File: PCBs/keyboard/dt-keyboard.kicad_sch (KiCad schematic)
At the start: 87 parts

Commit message: Fixed Keyboard
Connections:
- net Column 10: now also J1.14; no longer J1.10
- net Column 4: now also J1.8; no longer J1.4
- net Column 5: now also J1.9; no longer J1.5
- net Column 6: now also J1.10; no longer J1.6
- net Column 7: now also J1.11; no longer J1.7
- net Column 8: now also J1.12; no longer J1.8
- net Column 9: now also J1.13; no longer J1.9
- net Row 0: now also J1.4; no longer J1.11
- net Row 1: now also J1.5; no longer J1.12
- net Row 2: now also J1.6; no longer J1.13
- net Row 3: now also J1.7; no longer J1.14
- net GND: no longer names the net of J1.15 (MP)
- net GND: no longer J1.16 (MP)
- no-connect marks 0 -> 2
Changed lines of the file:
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@@
 		(color 0 0 0 0)
 	)
+	(no_connect
+		(at 35.56 137.16)
+	)
+	(no_connect
+		(at 35.56 185.42)
+	)
 	(wire
 		(pts
@@
 	(global_label "Row 3"
 		(shape input)
-		(at 43.18 179.07 0)
+		(at 43.18 161.29 0)
 		(fields_autoplaced yes)
 		(effects
@@
 		)
 		(property "Intersheetrefs" "${INTERSHEET_REFS}"
-			(at 52.0918 179.07 0)
+			(at 52.0918 161.29 0)
 			(effects
 				(font
@@
 	(global_label "Column 4"
 		(shape input)
-		(at 43.18 153.67 0)
+		(at 43.18 163.83 0)
 		(fields_autoplaced yes)
 		(effects
@@
 		)
 		(property "Intersheetrefs" "${INTERSHEET_REFS}"
-			(at 55.4178 153.67 0)
+			(at 55.4178 163.83 0)
 			(effects
 				(font
@@
 	(global_label "Row 2"
 		(shape input)
-		(at 43.18 176.53 0)
+		(at 43.18 158.75 0)
 		(fields_autoplaced yes)
 		(effects
@@
 		)
 		(property "Intersheetrefs" "${INTERSHEET_REFS}"
-			(at 52.0918 176.53 0)
+			(at 52.0918 158.75 0)
 			(effects
 				(font
@@
 	(global_label "Row 0"
 		(shape input)
-		(at 43.18 171.45 0)
+		(at 43.18 153.67 0)
 		(fields_autoplaced yes)
 		(effects
@@
 		)
 		(property "Intersheetrefs" "${INTERSHEET_REFS}"
-			(at 52.0918 171.45 0)
+			(at 52.0918 153.67 0)
 			(effects
 				(font
@@
 	(global_label "Column 6"
 		(shape input)
-		(at 43.18 158.75 0)
+		(at 43.18 168.91 0)
 		(fields_autoplaced yes)
 		(effects
@@
 		)
 		(property "Intersheetrefs" "${INTERSHEET_REFS}"
-			(at 55.4178 158.75 0)
+			(at 55.4178 168.91 0)
 			(effects
 				(font
@@
 	(global_label "Column 10"
 		(shape input)
-		(at 43.18 168.91 0)
+		(at 43.18 179.07 0)
 		(fields_autoplaced yes)
 		(effects
@@
 		)
 		(property "Intersheetrefs" "${INTERSHEET_REFS}"
-			(at 56.6273 168.91 0)
+			(at 56.6273 179.07 0)
 			(effects
 				(font
@@
 	(global_label "Row 1"
 		(shape input)
-		(at 43.18 173.99 0)
+		(at 43.18 156.21 0)
 		(fields_autoplaced yes)
 		(effects
@@
 		)
 		(property "Intersheetrefs" "${INTERSHEET_REFS}"
-			(at 52.0918 173.99 0)
+			(at 52.0918 156.21 0)
 			(effects
 				(font
@@
 	(global_label "Column 5"
 		(shape input)
-		(at 43.18 156.21 0)
+		(at 43.18 166.37 0)
 		(fields_autoplaced yes)
 		(effects
@@
 		)
 		(property "Intersheetrefs" "${INTERSHEET_REFS}"
-			(at 55.4178 156.21 0)
+			(at 55.4178 166.37 0)
 			(effects
 				(font
@@
 	(global_label "Column 7"
 		(shape input)
-		(at 43.18 161.29 0)
+		(at 43.18 171.45 0)
 		(fields_autoplaced yes)
 		(effects
@@
 		)
 		(property "Intersheetrefs" "${INTERSHEET_REFS}"
-			(at 55.4178 161.29 0)
+			(at 55.4178 171.45 0)
 			(effects
 				(font
@@
 	(global_label "Column 8"
 		(shape input)
-		(at 43.18 163.83 0)
+		(at 43.18 173.99 0)
 		(fields_autoplaced yes)
 		(effects
@@
 		)
 		(property "Intersheetrefs" "${INTERSHEET_REFS}"
-			(at 55.4178 163.83 0)
+			(at 55.4178 173.99 0)
 			(effects
 				(font
@@
 	(global_label "Column 9"
 		(shape input)
-		(at 43.18 166.37 0)
+		(at 43.18 176.53 0)
 		(fields_autoplaced yes)
 		(effects
@@
 		)
 		(property "Intersheetrefs" "${INTERSHEET_REFS}"
-			(at 55.4178 166.37 0)
+			(at 55.4178 176.53 0)
 			(effects
 				(font
@@
 	)
 	(symbol
-		(lib_id "power:GND")
-		(at 35.56 185.42 0)
-		(unit 1)
-		(exclude_from_sim no)
-		(in_bom yes)
-		(on_board yes)
-		(dnp no)
-		(fields_autoplaced yes)
-		(property "Reference" "#PWR01"
-			(at 35.56 191.77 0)
-			(effects
-				(font
-					(size 1.27 1.27)
-				)
-				(hide yes)
-			)
-		)
-		(property "Value" "GND"
-			(at 35.56 190.5 0)
-			(effects
-				(font
-					(size 1.27 1.27)
-				)
-			)
-		)
-		(property "Footprint" ""
-			(at 35.56 185.42 0)
-			(effects
-				(font
-					(size 1.27 1.27)
-				)
-				(hide yes)
-			)
-		)
-		(property "Datasheet" ""
-			(at 35.56 185.42 0)
-			(effects
-				(font
-					(size 1.27 1.27)
-				)
-				(hide yes)
-			)
-		)
-		(property "Description" "Power symbol creates a global label with name \"GND\" , ground"
-			(at 35.56 185.42 0)
-			(effects
-				(font
-					(size 1.27 1.27)
-				)
-				(hide yes)
-			)
-		)
-		(pin "1"
-		)
-		(instances
-			(project ""
-				(path "/a0f199ac-e5fb-4245-9c3a-54e045012dd6"
-					(reference "#PWR01")
-					(unit 1)
-				)
-			)
-		)
-	)
-	(symbol
 		(lib_id "ScottoKeebs:Placeholder_Diode")
 		(at 38.1 100.33 90)
@@
 					(unit 1)
 				)
-			)
-		)
-	)
-	(symbol
-		(lib_id "power:GND")
-		(at 35.56 137.16 180)
-		(unit 1)
-		(exclude_from_sim no)
-		(in_bom yes)
-		(on_board yes)
-		(dnp no)
-		(fields_autoplaced yes)
-		(property "Reference" "#PWR02"
-			(at 35.56 130.81 0)
-			(effects
-				(font
-					(size 1.27 1.27)
-				)
-				(hide yes)
-			)
-		)
-		(property "Value" "GND"
-			(at 35.56 132.08 0)
-			(effects
-				(font
-					(size 1.27 1.27)
-				)
-			)
-		)
-		(property "Footprint" ""
-			(at 35.56 137.16 0)
-			(effects
-				(font
-					(size 1.27 1.27)
-				)
-				(hide yes)
-			)
-		)
-		(property "Datasheet" ""
-			(at 35.56 137.16 0)
-			(effects
-				(font
-					(size 1.27 1.27)
-				)
-				(hide yes)
-			)
-		)
-		(property "Description" "Power symbol creates a global label with name \"GND\" , ground"
-			(at 35.56 137.16 0)
-			(effects
-				(font
-					(size 1.27 1.27)
-				)
-				(hide yes)
-			)
-		)
-		(pin "1"
-		)
-		(instances
-			(project "dt-keyboard"
-				(path "/a0f199ac-e5fb-4245-9c3a-54e045012dd6"
-					(reference "#PWR02")
-					(unit 1)
-				)

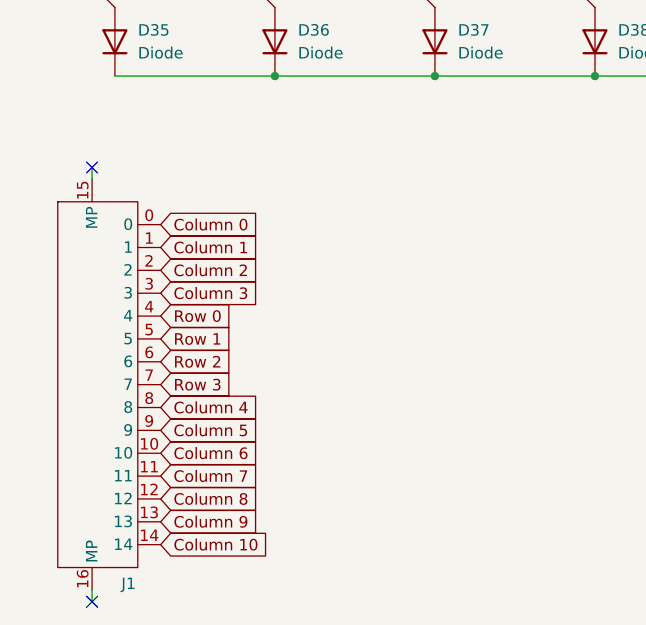
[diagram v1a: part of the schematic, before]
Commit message: Fixed Display Code + Added Peripherals on Schematic
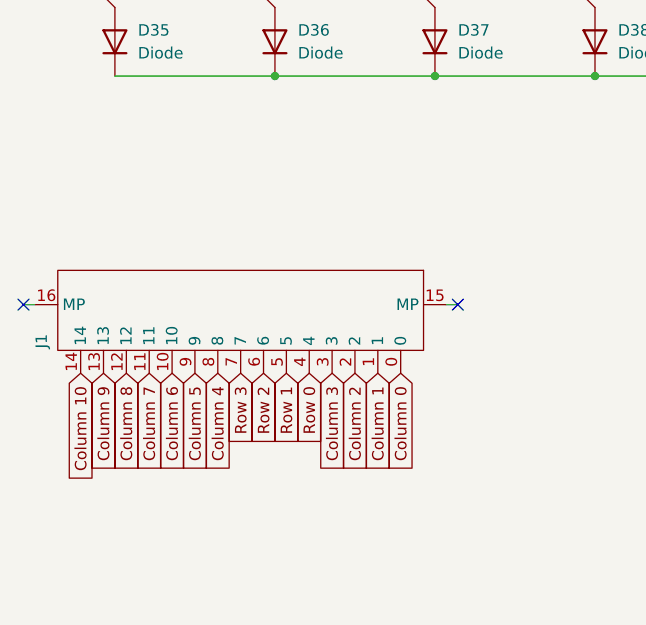
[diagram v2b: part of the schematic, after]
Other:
- moved on the sheet: J1
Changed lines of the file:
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@@
 	)
 	(no_connect
-		(at 35.56 137.16)
+		(at 76.2 152.4)
 	)
 	(no_connect
-		(at 35.56 185.42)
+		(at 27.94 152.4)
 	)
 	(wire
@@
 	(wire
 		(pts
-			(xy 35.56 185.42) (xy 35.56 184.15)
+			(xy 27.94 152.4) (xy 29.21 152.4)
 		)
 		(stroke
@@
 	(wire
 		(pts
-			(xy 35.56 137.16) (xy 35.56 138.43)
+			(xy 76.2 152.4) (xy 74.93 152.4)
 		)
 		(stroke
@@
 	(global_label "Row 3"
 		(shape input)
-		(at 43.18 161.29 0)
+		(at 52.07 160.02 270)
 		(fields_autoplaced yes)
 		(effects
@@
 				(size 1.27 1.27)
 			)
-			(justify left)
+			(justify right)
 		)
 		(property "Intersheetrefs" "${INTERSHEET_REFS}"
-			(at 52.0918 161.29 0)
+			(at 52.07 168.9318 90)
 			(effects
 				(font
 					(size 1.27 1.27)
 				)
-				(justify left)
+				(justify right)
 				(hide yes)
 			)
@@
 	(global_label "Column 4"
 		(shape input)
-		(at 43.18 163.83 0)
+		(at 49.53 160.02 270)
 		(fields_autoplaced yes)
 		(effects
@@
 				(size 1.27 1.27)
 			)
-			(justify left)
+			(justify right)
 		)
 		(property "Intersheetrefs" "${INTERSHEET_REFS}"
-			(at 55.4178 163.83 0)
+			(at 49.53 172.2578 90)
 			(effects
 				(font
 					(size 1.27 1.27)
 				)
-				(justify left)
+				(justify right)
 				(hide yes)
 			)
@@
 	(global_label "Column 3"
 		(shape input)
-		(at 43.18 151.13 0)
+		(at 62.23 160.02 270)
 		(fields_autoplaced yes)
 		(effects
@@
 				(size 1.27 1.27)
 			)
-			(justify left)
+			(justify right)
 		)
 		(property "Intersheetrefs" "${INTERSHEET_REFS}"
-			(at 55.4178 151.13 0)
+			(at 62.23 172.2578 90)
 			(effects
 				(font
 					(size 1.27 1.27)
 				)
-				(justify left)
+				(justify right)
 				(hide yes)
 			)
@@
 	(global_label "Row 2"
 		(shape input)
-		(at 43.18 158.75 0)
+		(at 54.61 160.02 270)
 		(fields_autoplaced yes)
 		(effects
@@
 				(size 1.27 1.27)
 			)
-			(justify left)
+			(justify right)
 		)
 		(property "Intersheetrefs" "${INTERSHEET_REFS}"
-			(at 52.0918 158.75 0)
+			(at 54.61 168.9318 90)
 			(effects
 				(font
 					(size 1.27 1.27)
 				)
-				(justify left)
+				(justify right)
 				(hide yes)
 			)
@@
 	(global_label "Column 0"
 		(shape input)
-		(at 43.18 143.51 0)
+		(at 69.85 160.02 270)
 		(fields_autoplaced yes)
 		(effects
@@
 				(size 1.27 1.27)
 			)
-			(justify left)
+			(justify right)
 		)
 		(property "Intersheetrefs" "${INTERSHEET_REFS}"
-			(at 55.4178 143.51 0)
+			(at 69.85 172.2578 90)
 			(effects
 				(font
 					(size 1.27 1.27)
 				)
-				(justify left)
+				(justify right)
 				(hide yes)
 			)
@@
 	(global_label "Row 0"
 		(shape input)
-		(at 43.18 153.67 0)
+		(at 59.69 160.02 270)
 		(fields_autoplaced yes)
 		(effects
@@
 				(size 1.27 1.27)
 			)
-			(justify left)
+			(justify right)
 		)
 		(property "Intersheetrefs" "${INTERSHEET_REFS}"
-			(at 52.0918 153.67 0)
+			(at 59.69 168.9318 90)
 			(effects
 				(font
 					(size 1.27 1.27)
 				)
-				(justify left)
+				(justify right)
 				(hide yes)
 			)
@@
 	(global_label "Column 6"
 		(shape input)
-		(at 43.18 168.91 0)
+		(at 44.45 160.02 270)
 		(fields_autoplaced yes)
 		(effects
@@
 				(size 1.27 1.27)
 			)
-			(justify left)
+			(justify right)
 		)
 		(property "Intersheetrefs" "${INTERSHEET_REFS}"
-			(at 55.4178 168.91 0)
+			(at 44.45 172.2578 90)
 			(effects
 				(font
 					(size 1.27 1.27)
 				)
-				(justify left)
+				(justify right)
 				(hide yes)
 			)
@@
 	(global_label "Column 1"
 		(shape input)
-		(at 43.18 146.05 0)
+		(at 67.31 160.02 270)
 		(fields_autoplaced yes)
 		(effects
@@
 				(size 1.27 1.27)
 			)
-			(justify left)
+			(justify right)
 		)
 		(property "Intersheetrefs" "${INTERSHEET_REFS}"
-			(at 55.4178 146.05 0)
+			(at 67.31 172.2578 90)
 			(effects
 				(font
 					(size 1.27 1.27)
 				)
-				(justify left)
+				(justify right)
 				(hide yes)
 			)
@@
 	(global_label "Column 10"
 		(shape input)
-		(at 43.18 179.07 0)
+		(at 34.29 160.02 270)
 		(fields_autoplaced yes)
 		(effects
@@
 				(size 1.27 1.27)
 			)
-			(justify left)
+			(justify right)
 		)
 		(property "Intersheetrefs" "${INTERSHEET_REFS}"
-			(at 56.6273 179.07 0)
+			(at 34.29 173.4673 90)
 			(effects
 				(font
 					(size 1.27 1.27)
 				)
-				(justify left)
+				(justify right)
 				(hide yes)
 			)
@@
 	(global_label "Row 1"
 		(shape input)
-		(at 43.18 156.21 0)
+		(at 57.15 160.02 270)
 		(fields_autoplaced yes)
 		(effects
@@
 				(size 1.27 1.27)
 			)
-			(justify left)
+			(justify right)
 		)
 		(property "Intersheetrefs" "${INTERSHEET_REFS}"
-			(at 52.0918 156.21 0)
+			(at 57.15 168.9318 90)
 			(effects
 				(font
 					(size 1.27 1.27)
 				)
-				(justify left)
+				(justify right)
 				(hide yes)
 			)
@@
 	(global_label "Column 5"
 		(shape input)
-		(at 43.18 166.37 0)
+		(at 46.99 160.02 270)
 		(fields_autoplaced yes)
 		(effects
@@
 				(size 1.27 1.27)
 			)
-			(justify left)
+			(justify right)
 		)
 		(property "Intersheetrefs" "${INTERSHEET_REFS}"
-			(at 55.4178 166.37 0)
+			(at 46.99 172.2578 90)
 			(effects
 				(font
 					(size 1.27 1.27)
 				)
-				(justify left)
+				(justify right)
 				(hide yes)
 			)
@@
 	(global_label "Column 2"
 		(shape input)
-		(at 43.18 148.59 0)
+		(at 64.77 160.02 270)
 		(fields_autoplaced yes)
 		(effects
@@
 				(size 1.27 1.27)
 			)
-			(justify left)
+			(justify right)
 		)
 		(property "Intersheetrefs" "${INTERSHEET_REFS}"
-			(at 55.4178 148.59 0)
+			(at 64.77 172.2578 90)
 			(effects
 				(font
 					(size 1.27 1.27)
 				)
-				(justify left)
+				(justify right)
 				(hide yes)
 			)
@@
 	(global_label "Column 7"
 		(shape input)
-		(at 43.18 171.45 0)
+		(at 41.91 160.02 270)
 		(fields_autoplaced yes)
 		(effects
@@
 				(size 1.27 1.27)
 			)
-			(justify left)
+			(justify right)
 		)
 		(property "Intersheetrefs" "${INTERSHEET_REFS}"
-			(at 55.4178 171.45 0)
+			(at 41.91 172.2578 90)
 			(effects
 				(font
 					(size 1.27 1.27)
 				)
-				(justify left)
+				(justify right)
 				(hide yes)
 			)
@@
 	(global_label "Column 8"
 		(shape input)
-		(at 43.18 173.99 0)
+		(at 39.37 160.02 270)
 		(fields_autoplaced yes)
 		(effects
@@
 				(size 1.27 1.27)
 			)
-			(justify left)
+			(justify right)
 		)
 		(property "Intersheetrefs" "${INTERSHEET_REFS}"
-			(at 55.4178 173.99 0)
+			(at 39.37 172.2578 90)
 			(effects
 				(font
 					(size 1.27 1.27)
 				)
-				(justify left)
+				(justify right)
 				(hide yes)
 			)
@@
 	(global_label "Column 9"
 		(shape input)
-		(at 43.18 176.53 0)
+		(at 36.83 160.02 270)
 		(fields_autoplaced yes)
 		(effects
@@
 				(size 1.27 1.27)
 			)
-			(justify left)
+			(justify right)
 		)
 		(property "Intersheetrefs" "${INTERSHEET_REFS}"
-			(at 55.4178 176.53 0)
+			(at 36.83 172.2578 90)
 			(effects
 				(font
 					(size 1.27 1.27)
 				)
-				(justify left)
+				(justify right)
 				(hide yes)
 			)
@@
 	(symbol
 		(lib_id "Custom:FPC-1.0FX-15PWCR-H20")
-		(at 31.75 181.61 0)
+		(at 31.75 148.59 270)
 		(unit 1)
 		(exclude_from_sim no)
@@
 		(fields_autoplaced yes)
 		(property "Reference" "J1"
-			(at 39.624 184.15 0)
+			(at 29.21 156.464 0)
 			(do_not_autoplace yes)
 			(effects
@@
 		)
 		(property "Value" "~"
-			(at 31.75 181.61 0)
+			(at 31.75 148.59 0)
 			(effects
 				(font
@@
 		)
 		(property "Footprint" "Custom:FPC_15"
-			(at 36.576 183.134 0)
+			(at 30.226 153.416 0)
 			(effects
 				(font
@@
 		)
 		(property "Datasheet" ""
-			(at 31.75 181.61 0)
+			(at 31.75 148.59 0)
 			(effects
 				(font
@@
 		)
 		(property "Description" ""
-			(at 31.75 181.61 0)
+			(at 31.75 148.59 0)
 			(effects
 				(font

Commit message: Layouting + Deep Sleep Tests
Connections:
- net Column 3: now also J1.7; no longer J1.3
- net Row 0: now also J1.3; no longer J1.4
- net Row 1: now also J1.4; no longer J1.5
- net Row 2: now also J1.5; no longer J1.6
- net Row 3: now also J1.6; no longer J1.7

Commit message: Verification
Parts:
- added H1, H2: MountingHole_Pad, MountingHole:MountingHole_3.2mm_M3_Pad_TopBottom, symbol Mechanical:MountingHole_Pad
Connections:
- no-connect marks 2 -> 4
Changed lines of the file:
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@@
 	)
 	(no_connect
+		(at 87.63 154.94)
+	)
+	(no_connect
 		(at 27.94 152.4)
 	)
+	(no_connect
+		(at 87.63 163.83)
+	)
 	(wire
 		(pts
@@
 	)
 	(symbol
+		(lib_id "Mechanical:MountingHole_Pad")
+		(at 87.63 152.4 0)
+		(unit 1)
+		(exclude_from_sim no)
+		(in_bom no)
+		(on_board yes)
+		(dnp no)
+		(fields_autoplaced yes)
+		(property "Reference" "H1"
+			(at 90.17 149.8599 0)
+			(effects
+				(font
+					(size 1.27 1.27)
+				)
+				(justify left)
+			)
+		)
+		(property "Value" "MountingHole_Pad"
+			(at 90.17 152.3999 0)
+			(effects
+				(font
+					(size 1.27 1.27)
+				)
+				(justify left)
+			)
+		)
+		(property "Footprint" "MountingHole:MountingHole_3.2mm_M3_Pad_TopBottom"
+			(at 87.63 152.4 0)
+			(effects
+				(font
+					(size 1.27 1.27)
+				)
+				(hide yes)
+			)
+		)
+		(property "Datasheet" "~"
+			(at 87.63 152.4 0)
+			(effects
+				(font
+					(size 1.27 1.27)
+				)
+				(hide yes)
+			)
+		)
+		(property "Description" "Mounting Hole with connection"
+			(at 87.63 152.4 0)
+			(effects
+				(font
+					(size 1.27 1.27)
+				)
+				(hide yes)
+			)
+		)
+		(pin "1"
+		)
+		(instances
+			(project ""
+				(path "/a0f199ac-e5fb-4245-9c3a-54e045012dd6"
+					(reference "H1")
+					(unit 1)
+				)
+			)
+		)
+	)
+	(symbol
 		(lib_id "ScottoKeebs:Placeholder_Keyswitch")
 		(at 88.9 93.98 0)
@@
 					(unit 1)
 				)
+			)
+		)
+	)
+	(symbol
+		(lib_id "Mechanical:MountingHole_Pad")
+		(at 87.63 161.29 0)
+		(unit 1)
+		(exclude_from_sim no)
+		(in_bom no)
+		(on_board yes)
+		(dnp no)
+		(fields_autoplaced yes)
+		(property "Reference" "H2"
+			(at 90.17 158.7499 0)
+			(effects
+				(font
+					(size 1.27 1.27)
+				)
+				(justify left)
+			)
+		)
+		(property "Value" "MountingHole_Pad"
+			(at 90.17 161.2899 0)
+			(effects
+				(font
+					(size 1.27 1.27)
+				)
+				(justify left)
+			)
+		)
+		(property "Footprint" "MountingHole:MountingHole_3.2mm_M3_Pad_TopBottom"
+			(at 87.63 161.29 0)
+			(effects
+				(font
+					(size 1.27 1.27)
+				)
+				(hide yes)
+			)
+		)
+		(property "Datasheet" "~"
+			(at 87.63 161.29 0)
+			(effects
+				(font
+					(size 1.27 1.27)
+				)
+				(hide yes)
+			)
+		)
+		(property "Description" "Mounting Hole with connection"
+			(at 87.63 161.29 0)
+			(effects
+				(font
+					(size 1.27 1.27)
+				)
+				(hide yes)
+			)
+		)
+		(pin "1"
+		)
+		(instances
+			(project "dt-keyboard"
+				(path "/a0f199ac-e5fb-4245-9c3a-54e045012dd6"
+					(reference "H2")
+					(unit 1)
+				)
